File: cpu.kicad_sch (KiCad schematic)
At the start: 36 parts, among them IC901 HUC6280, IC906 LC3664BML-10, Q901 L6

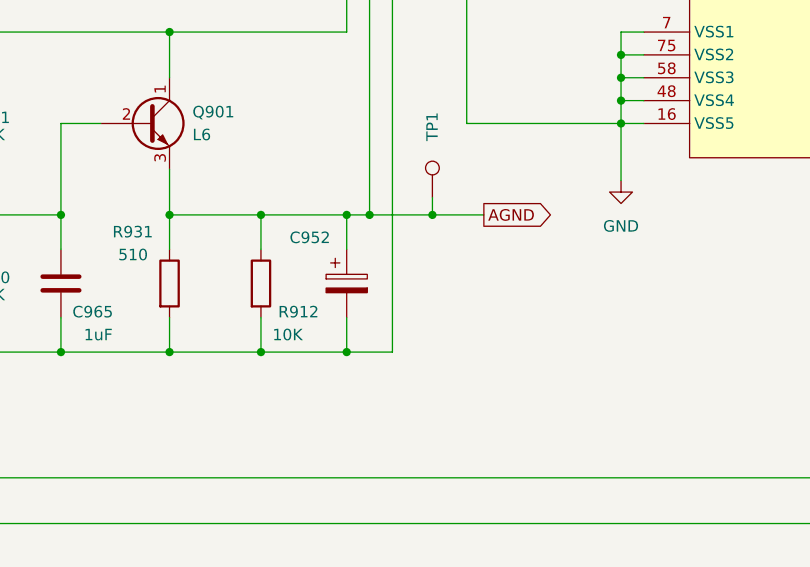
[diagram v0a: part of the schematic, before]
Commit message: Add more capacitor values, rearrange some schematics.
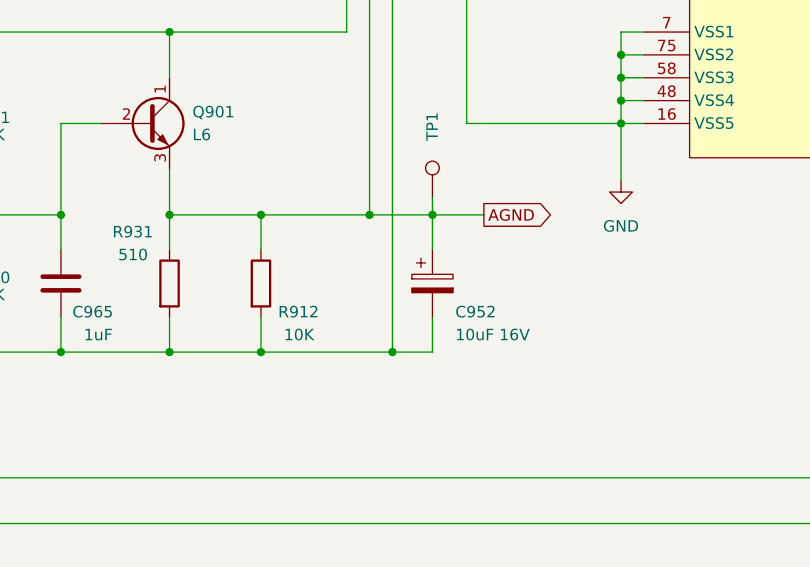
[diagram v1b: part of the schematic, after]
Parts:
- C952: value ~ -> 10uF 16V
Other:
- moved on the sheet: C952
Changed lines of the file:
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@@
   (junction (at 190.5 158.75) (diameter 0) (color 0 0 0 0)
   )
+  (junction (at 165.1 207.01) (diameter 0) (color 0 0 0 0)
+  )
   (junction (at 262.89 48.26) (diameter 0) (color 0 0 0 0)
   )
@@
   (junction (at 95.25 214.63) (diameter 0) (color 0 0 0 0)
   )
-  (junction (at 160.02 191.77) (diameter 0) (color 0 0 0 0)
-  )
   (junction (at 241.3 123.19) (diameter 0) (color 0 0 0 0)
   )
@@
   )
   (junction (at 158.75 69.85) (diameter 0) (color 0 0 0 0)
-  )
-  (junction (at 160.02 207.01) (diameter 0) (color 0 0 0 0)
   )
   (junction (at 169.545 191.77) (diameter 0) (color 0 0 0 0)
@@
     (stroke (width 0) (type default))
   )
-  (wire (pts (xy 162.56 191.77) (xy 169.545 191.77))
-    (stroke (width 0) (type default))
-  )
   (wire (pts (xy 322.58 105.41) (xy 322.58 110.49))
     (stroke (width 0) (type default))
@@
     (stroke (width 0) (type default))
   )
+  (wire (pts (xy 169.545 207.01) (xy 165.1 207.01))
+    (stroke (width 0) (type default))
+  )
   (wire (pts (xy 193.04 125.73) (xy 100.33 125.73))
     (stroke (width 0) (type default))
@@
     (stroke (width 0) (type default))
   )
-  (wire (pts (xy 150.495 207.01) (xy 160.02 207.01))
-    (stroke (width 0) (type default))
-  )
   (wire (pts (xy 144.78 254) (xy 144.78 251.46))
     (stroke (width 0) (type default))
@@
     (stroke (width 0) (type default))
   )
-  (wire (pts (xy 160.02 191.77) (xy 162.56 191.77))
+  (wire (pts (xy 150.495 191.77) (xy 162.56 191.77))
     (stroke (width 0) (type default))
   )
@@
     (stroke (width 0) (type default))
   )
-  (wire (pts (xy 160.02 191.77) (xy 160.02 195.58))
+  (wire (pts (xy 169.545 191.77) (xy 169.545 195.58))
     (stroke (width 0) (type default))
   )
@@
     (stroke (width 0) (type default))
   )
+  (wire (pts (xy 169.545 191.77) (xy 162.56 191.77))
+    (stroke (width 0) (type default))
+  )
   (bus (pts (xy 238.76 102.87) (xy 238.76 100.33))
     (stroke (width 0) (type default))
@@
     (stroke (width 0) (type default))
   )
-  (wire (pts (xy 160.02 207.01) (xy 165.1 207.01))
+  (wire (pts (xy 150.495 207.01) (xy 165.1 207.01))
     (stroke (width 0) (type default))
   )
@@
     (stroke (width 0) (type default))
   )
-  (wire (pts (xy 150.495 191.77) (xy 160.02 191.77))
-    (stroke (width 0) (type default))
-  )
   (wire (pts (xy 167.64 27.94) (xy 167.64 54.61))
     (stroke (width 0) (type default))
   )
-  (wire (pts (xy 160.02 203.2) (xy 160.02 207.01))
+  (wire (pts (xy 169.545 203.2) (xy 169.545 207.01))
     (stroke (width 0) (type default))
   )
@@
       (effects (font (size 1.27 1.27)) (justify left))
     )
-    (property "Value" "10K" (at 151.765 205.105 0)
+    (property "Value" "10K" (at 153.035 205.105 0)
       (effects (font (size 1.27 1.27)) (justify left))
     )
@@
     )
   )
-  (symbol (lib_id "Device:C_Polarized") (at 160.02 199.39 0) (unit 1)
+  (symbol (lib_id "Device:C_Polarized") (at 169.545 199.39 0) (unit 1)
     (in_bom yes) (on_board yes) (dnp no)
-    (property "Reference" "C952" (at 153.67 194.31 0)
-      (effects (font (size 1.27 1.27)) (justify left))
-    )
-    (property "Value" "~" (at 163.83 199.771 0)
-      (effects (font (size 1.27 1.27)) (justify left))
-    )
-    (property "Footprint" "A-PCENGINE:CP_2010_XL" (at 160.9852 203.2 0)
-      (effects (font (size 1.27 1.27)) hide)
-    )
-    (property "Datasheet" "~" (at 160.02 199.39 0)
-      (effects (font (size 1.27 1.27)) hide)
-    )
+    (property "Reference" "C952" (at 172.085 202.565 0)
+      (effects (font (size 1.27 1.27)) (justify left))
+    )
+    (property "Value" "10uF 16V" (at 172.085 205.105 0)
+      (effects (font (size 1.27 1.27)) (justify left))
+    )
+    (property "Footprint" "A-PCENGINE:CP_2010_XL" (at 170.5102 203.2 0)
+      (effects (font (size 1.27 1.27)) hide)
+    )
+    (property "Datasheet" "~" (at 169.545 199.39 0)
+      (effects (font (size 1.27 1.27)) hide)
+    )

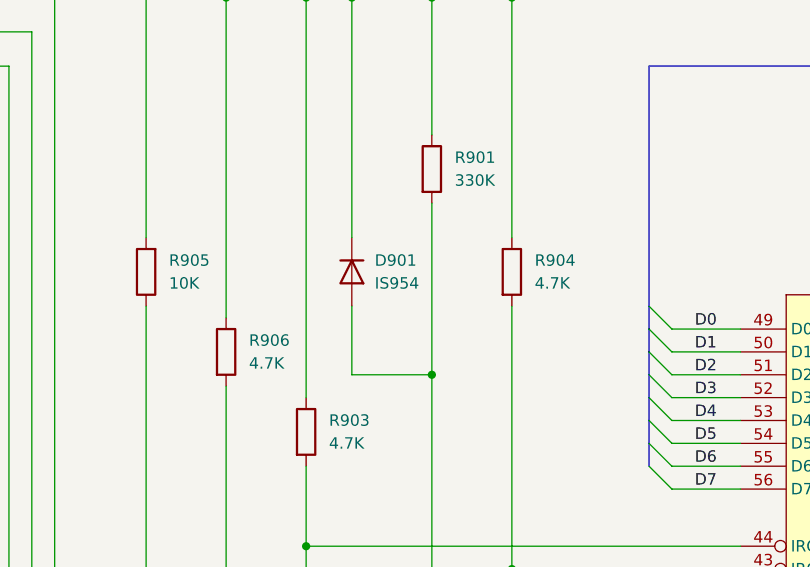
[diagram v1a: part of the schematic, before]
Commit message: Add markings for SMD Ds and Qs.
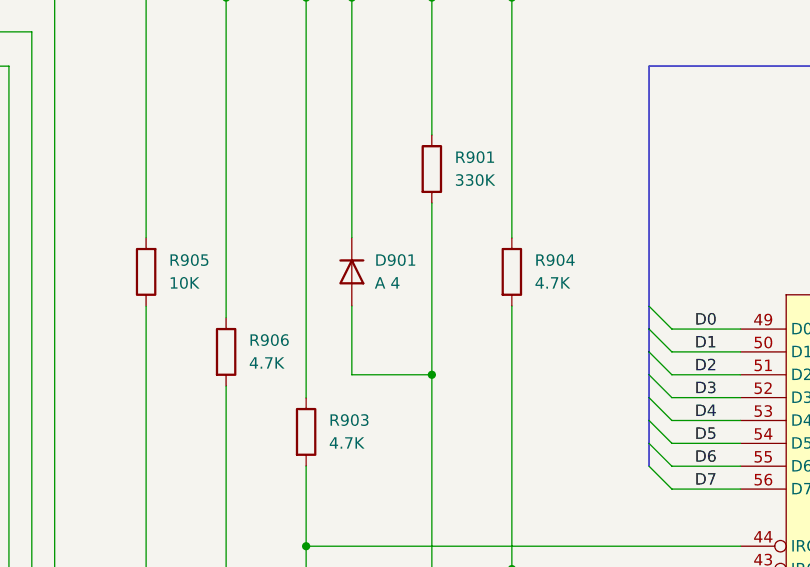
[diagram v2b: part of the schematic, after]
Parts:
- D901: value IS954 -> A 4
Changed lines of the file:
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@@
       (effects (font (size 1.27 1.27)) (justify left))
     )
-    (property "Value" "IS954" (at 152.4 59.69 90)
+    (property "Value" "A 4" (at 152.4 59.69 90)
       (effects (font (size 1.27 1.27)) (justify left))
     )

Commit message: More schematic clean-up/annotation.
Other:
- company: (none) -> By Cosam
- title: PC Engine CPU and RAM -> PC Engine Duo CPU and RAM
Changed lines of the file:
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@@
   (paper "A3")
   (title_block
-    (title "PC Engine CPU and RAM")
-    (date "2023-11-01")
-    (rev "1.0")
-    (comment 1 "Reverse engineered from original PWA-3285-A board by Cosam")
-    (comment 3 "WORK IN PROGRESS")
+    (title "PC Engine Duo CPU and RAM")
+    (date "2023-11-03")
+    (rev "1.1")
+    (company "By Cosam")
+    (comment 1 "https://github.com/Board-Folk/PC-Engine-Duo")
+    (comment 2 "For contributions or corrections please visit:")
+    (comment 3 "Additional parts reverse engineered from original PWA-3285-A board.")
+    (comment 4 "Parts common to PC Engine adapted from TurboGrafx-16 schematics.")
   )
   (junction (at 95.25 184.15) (diameter 0) (color 0 0 0 0)

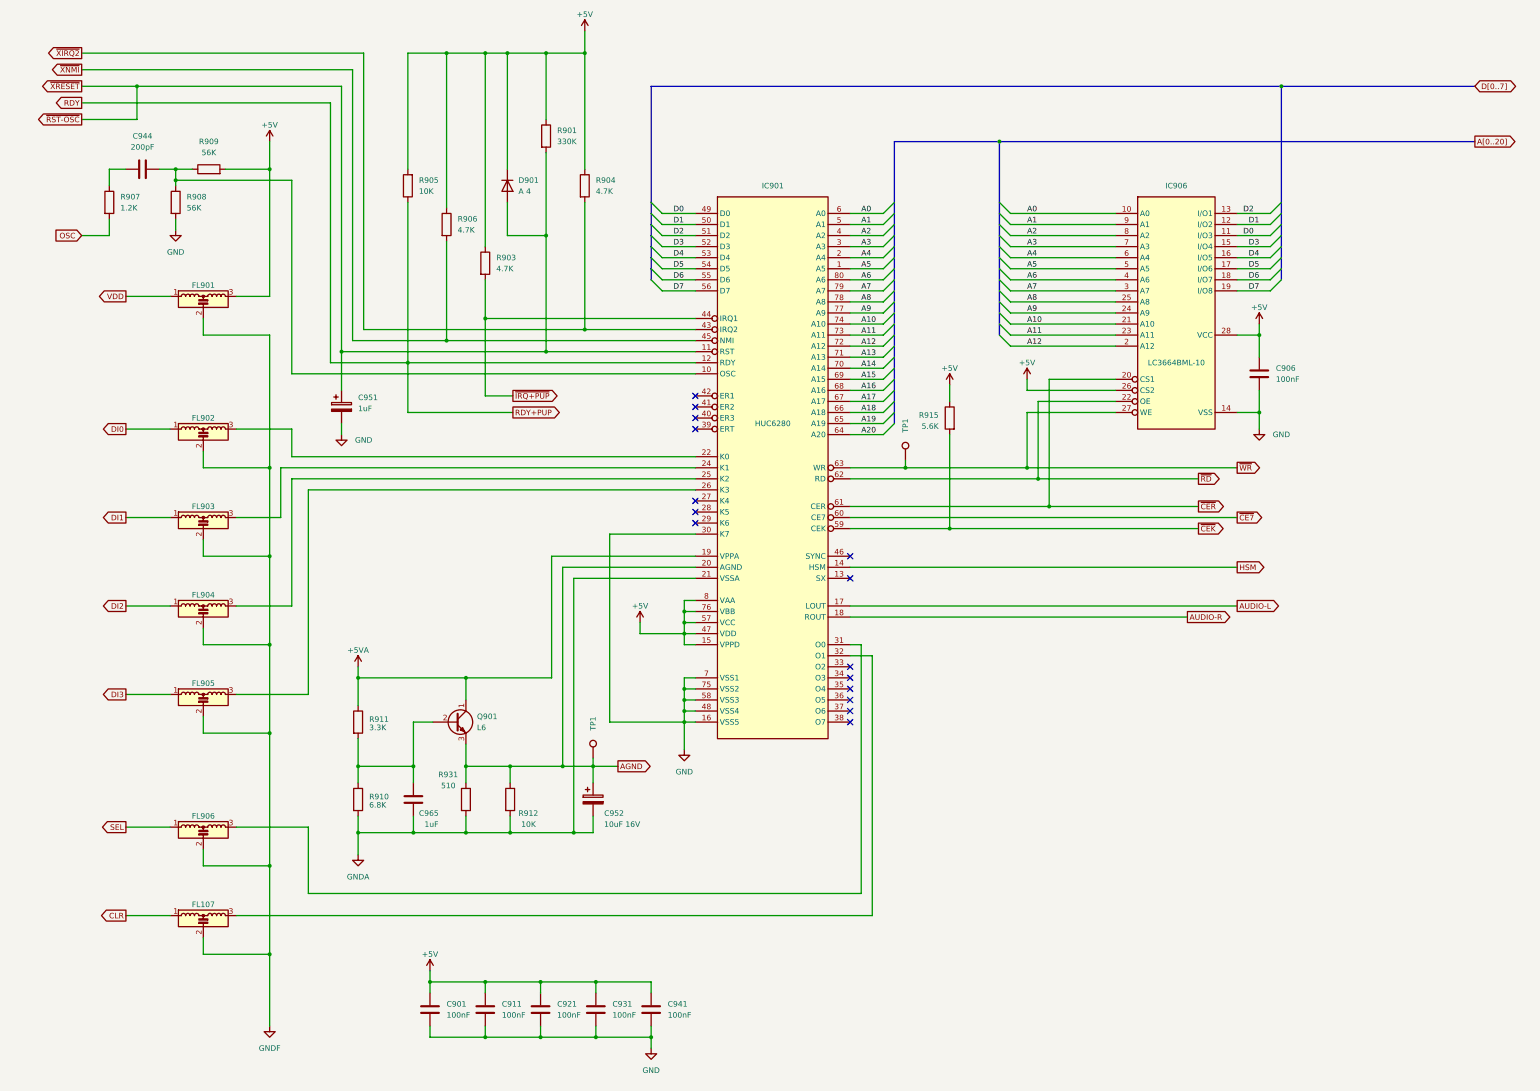
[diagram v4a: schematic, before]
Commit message: Minor schematic/silkscreen changes.
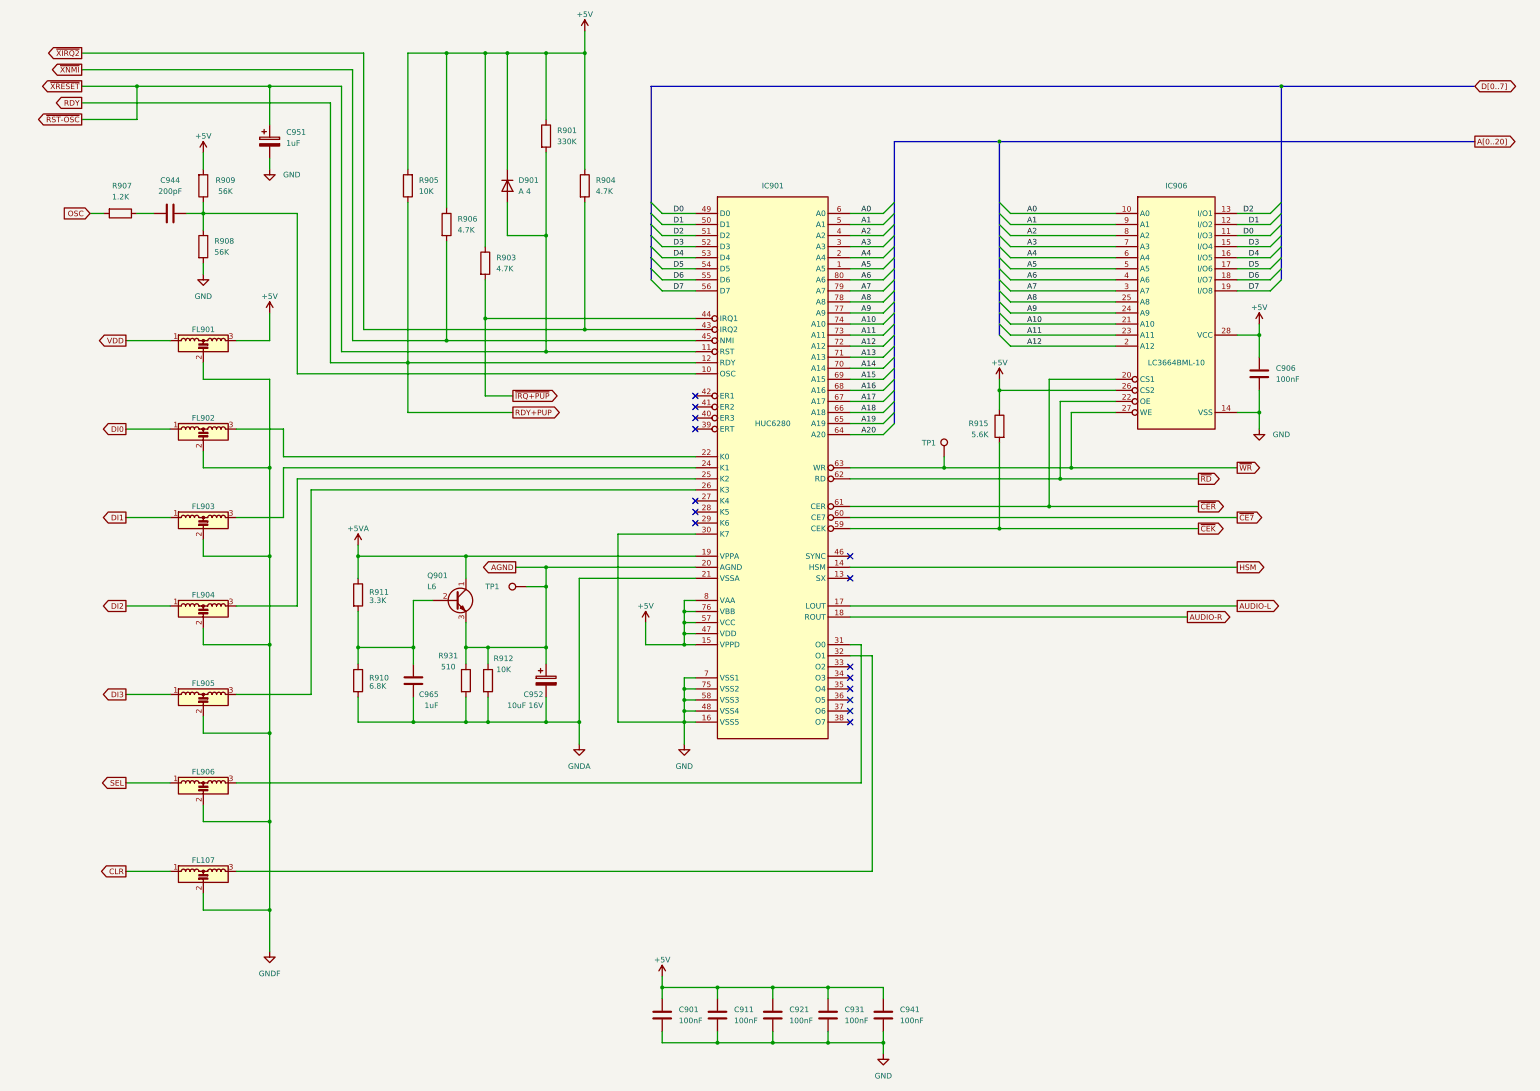
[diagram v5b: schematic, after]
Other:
- moved on the sheet: C901, C911, C921, C931, C941, C944, C951, C952, C965, FL107, FL901, FL906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
